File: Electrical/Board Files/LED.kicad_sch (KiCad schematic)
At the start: 22 parts, among them M1 Motor_DC, Q3 BSS138, Q4 BSS138, Q5 BSS138, Q6 BSS138, Q7 BSS138, Q8 BSS138

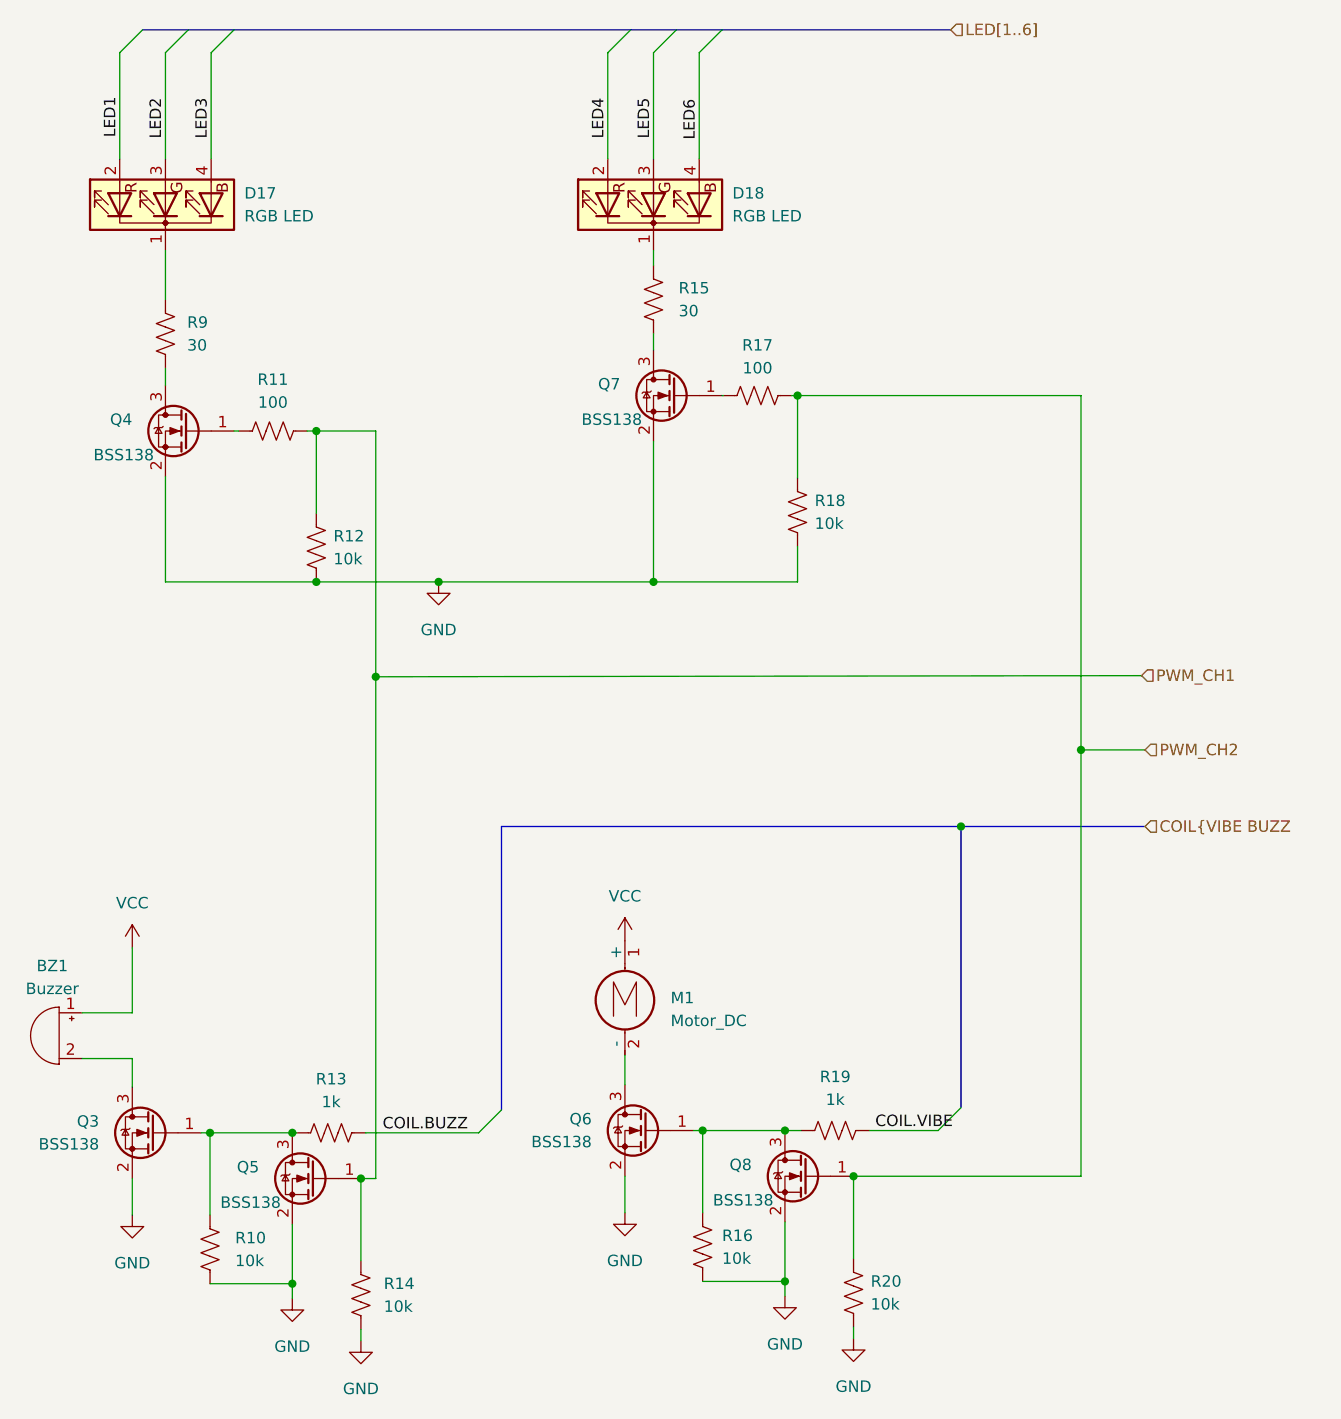
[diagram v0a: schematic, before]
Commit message: Removed unnecessary FETs
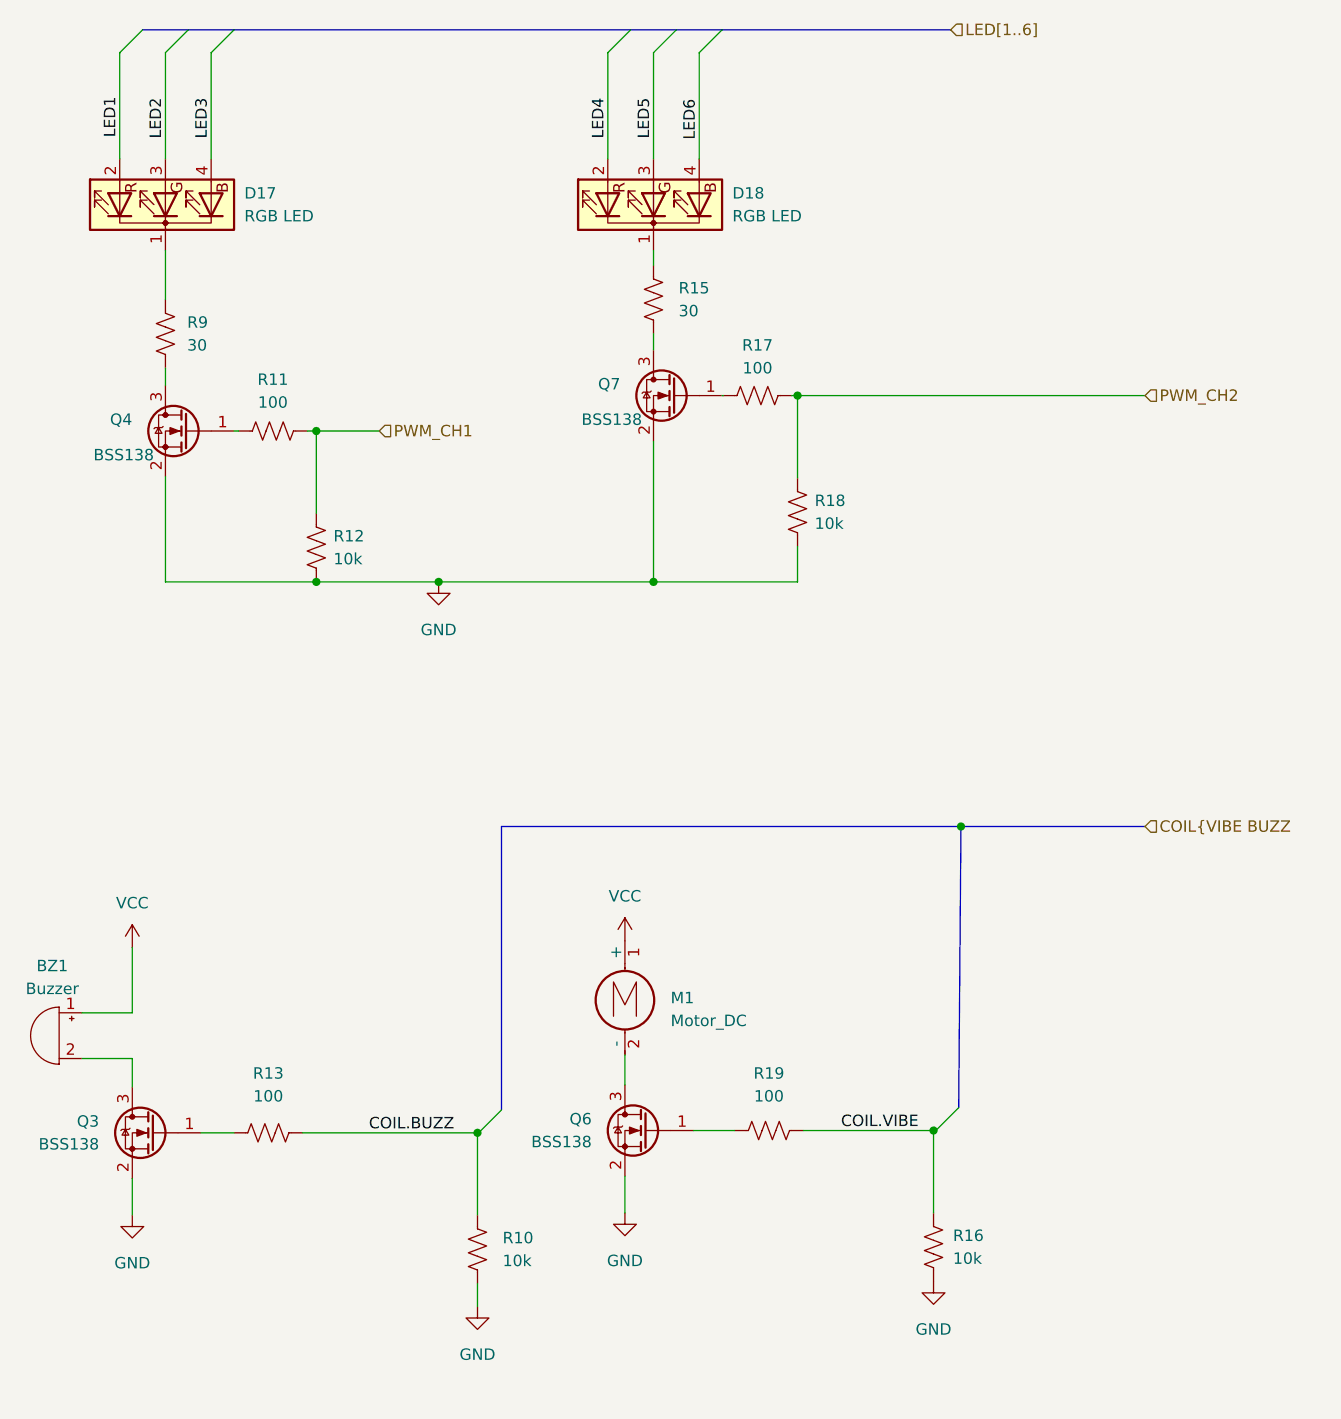
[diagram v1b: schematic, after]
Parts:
- removed Q5, Q8: BSS138, Package_TO_SOT_SMD:SOT-23, symbol Transistor_FET:BSS138
- removed R14, R20: 10k, Resistor_SMD:R_0603_1608Metric, symbol Device:R_US
- R13, R19: value 1k -> 100
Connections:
- net COIL.BUZZ: now also R10.1
- net COIL.VIBE: now also R16.1
- net at Q3.1 (G), R13.1: no longer R10.1
- net at Q6.1 (G), R19.1: no longer R16.1
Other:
- moved on the sheet: R10, R13, R16, R19

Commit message: Adding footprints
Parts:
- BZ1: footprint (none) -> Connector_PinSocket_2.00mm:PinSocket_1x02_P2.00mm_Vertical
- M1: footprint (none) -> Connector_PinSocket_2.54mm:PinSocket_1x04_P2.54mm_Vertical
- renumbered Q6 to Q5, Q7 to Q6, R9 to R15, R13 to R16, R11 to R17, R12 to R18, R10 to R19, R15 to R20, R17 to R21, R19 to R22, R18 to R23, R16 to R24
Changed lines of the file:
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@@
   (symbol (lib_id "Transistor_FET:BSS138") (at 107.442 64.389 0) (mirror y) (unit 1)
     (in_bom yes) (on_board yes)
-    (property "Reference" "Q7" (id 0) (at 101.219 63.1189 0)
+    (property "Reference" "Q6" (id 0) (at 101.219 63.1189 0)
       (effects (font (size 1.27 1.27)) (justify left))
     )
@@
   (symbol (lib_id "power:GND") (at 136.017 162.814 0) (unit 1)
     (in_bom yes) (on_board yes) (fields_autoplaced)
-    (property "Reference" "#PWR?" (id 0) (at 136.017 169.164 0)
+    (property "Reference" "#PWR044" (id 0) (at 136.017 169.164 0)
       (effects (font (size 1.27 1.27)) hide)
     )
@@
   (symbol (lib_id "power:VCC") (at 101.727 124.968 0) (unit 1)
     (in_bom yes) (on_board yes) (fields_autoplaced)
-    (property "Reference" "#PWR035" (id 0) (at 101.727 128.778 0)
+    (property "Reference" "#PWR042" (id 0) (at 101.727 128.778 0)
       (effects (font (size 1.27 1.27)) hide)
     )
@@
   (symbol (lib_id "Device:R_US") (at 136.017 159.004 0) (unit 1)
     (in_bom yes) (on_board yes) (fields_autoplaced)
-    (property "Reference" "R16" (id 0) (at 138.176 157.7339 0)
+    (property "Reference" "R24" (id 0) (at 138.176 157.7339 0)
       (effects (font (size 1.27 1.27)) (justify left))
     )
@@
   (symbol (lib_id "Transistor_FET:BSS138") (at 104.267 146.05 0) (mirror y) (unit 1)
     (in_bom yes) (on_board yes) (fields_autoplaced)
-    (property "Reference" "Q6" (id 0) (at 98.044 144.7799 0)
+    (property "Reference" "Q5" (id 0) (at 98.044 144.7799 0)
       (effects (font (size 1.27 1.27)) (justify left))
     )
@@
   (symbol (lib_id "power:GND") (at 85.344 165.608 0) (unit 1)
     (in_bom yes) (on_board yes) (fields_autoplaced)
-    (property "Reference" "#PWR032" (id 0) (at 85.344 171.958 0)
+    (property "Reference" "#PWR041" (id 0) (at 85.344 171.958 0)
       (effects (font (size 1.27 1.27)) hide)
     )
@@
   (symbol (lib_id "power:GND") (at 101.727 155.194 0) (unit 1)
     (in_bom yes) (on_board yes) (fields_autoplaced)
-    (property "Reference" "#PWR036" (id 0) (at 101.727 161.544 0)
+    (property "Reference" "#PWR043" (id 0) (at 101.727 161.544 0)
       (effects (font (size 1.27 1.27)) hide)
     )
@@
     (property "Reference" "BZ1" (id 0) (at 38.1 127.762 0))
     (property "Value" "Buzzer" (id 1) (at 38.1 130.302 0))
-    (property "Footprint" "" (id 2) (at 39.497 132.969 90)
+    (property "Footprint" "Connector_PinSocket_2.00mm:PinSocket_1x02_P2.00mm_Vertical" (id 2) (at 39.497 132.969 90)
       (effects (font (size 1.27 1.27)) hide)
     )
@@
   (symbol (lib_id "Device:R_US") (at 120.904 77.343 0) (unit 1)
     (in_bom yes) (on_board yes) (fields_autoplaced)
-    (property "Reference" "R18" (id 0) (at 122.809 76.0729 0)
+    (property "Reference" "R23" (id 0) (at 122.809 76.0729 0)
       (effects (font (size 1.27 1.27)) (justify left))
     )
@@
   (symbol (lib_id "Device:R_US") (at 104.902 53.721 0) (unit 1)
     (in_bom yes) (on_board yes) (fields_autoplaced)
-    (property "Reference" "R15" (id 0) (at 107.696 52.4509 0)
+    (property "Reference" "R20" (id 0) (at 107.696 52.4509 0)
       (effects (font (size 1.27 1.27)) (justify left))
     )
@@
   (symbol (lib_id "Device:R_US") (at 85.344 159.258 0) (unit 1)
     (in_bom yes) (on_board yes) (fields_autoplaced)
-    (property "Reference" "R10" (id 0) (at 88.138 157.9879 0)
+    (property "Reference" "R19" (id 0) (at 88.138 157.9879 0)
       (effects (font (size 1.27 1.27)) (justify left))
     )
@@
   (symbol (lib_id "Device:R_US") (at 50.673 57.531 0) (unit 1)
     (in_bom yes) (on_board yes) (fields_autoplaced)
-    (property "Reference" "R9" (id 0) (at 53.086 56.2609 0)
+    (property "Reference" "R15" (id 0) (at 53.086 56.2609 0)
       (effects (font (size 1.27 1.27)) (justify left))
     )
@@
   (symbol (lib_id "Device:R_US") (at 67.437 81.28 0) (unit 1)
     (in_bom yes) (on_board yes) (fields_autoplaced)
-    (property "Reference" "R12" (id 0) (at 69.342 80.0099 0)
+    (property "Reference" "R18" (id 0) (at 69.342 80.0099 0)
       (effects (font (size 1.27 1.27)) (justify left))
     )
@@
   (symbol (lib_id "Device:R_US") (at 116.459 64.389 90) (unit 1)
     (in_bom yes) (on_board yes) (fields_autoplaced)
-    (property "Reference" "R17" (id 0) (at 116.459 58.801 90))
+    (property "Reference" "R21" (id 0) (at 116.459 58.801 90))
     (property "Value" "100" (id 1) (at 116.459 61.341 90))
     (property "Footprint" "Resistor_SMD:R_0603_1608Metric" (id 2) (at 116.713 63.373 90)
@@
   (symbol (lib_id "power:VCC") (at 46.99 125.73 0) (unit 1)
     (in_bom yes) (on_board yes) (fields_autoplaced)
-    (property "Reference" "#PWR030" (id 0) (at 46.99 129.54 0)
+    (property "Reference" "#PWR038" (id 0) (at 46.99 129.54 0)
       (effects (font (size 1.27 1.27)) hide)
     )
@@
   (symbol (lib_id "Device:R_US") (at 62.103 146.304 90) (unit 1)
     (in_bom yes) (on_board yes) (fields_autoplaced)
-    (property "Reference" "R13" (id 0) (at 62.103 139.7 90))
+    (property "Reference" "R16" (id 0) (at 62.103 139.7 90))
     (property "Value" "100" (id 1) (at 62.103 142.24 90))
     (property "Footprint" "Resistor_SMD:R_0603_1608Metric" (id 2) (at 62.357 145.288 90)
@@
   (symbol (lib_id "power:GND") (at 46.99 155.448 0) (unit 1)
     (in_bom yes) (on_board yes) (fields_autoplaced)
-    (property "Reference" "#PWR031" (id 0) (at 46.99 161.798 0)
+    (property "Reference" "#PWR039" (id 0) (at 46.99 161.798 0)
       (effects (font (size 1.27 1.27)) hide)
     )
@@
   (symbol (lib_id "Device:R_US") (at 62.611 68.326 90) (unit 1)
     (in_bom yes) (on_board yes) (fields_autoplaced)
-    (property "Reference" "R11" (id 0) (at 62.611 62.611 90))
+    (property "Reference" "R17" (id 0) (at 62.611 62.611 90))
     (property "Value" "100" (id 1) (at 62.611 65.151 90))
     (property "Footprint" "Resistor_SMD:R_0603_1608Metric" (id 2) (at 62.865 67.31 90)
@@
   (symbol (lib_id "Device:R_US") (at 117.729 146.05 90) (unit 1)
     (in_bom yes) (on_board yes) (fields_autoplaced)
-    (property "Reference" "R19" (id 0) (at 117.729 139.7 90))
+    (property "Reference" "R22" (id 0) (at 117.729 139.7 90))
     (property "Value" "100" (id 1) (at 117.729 142.24 90))
     (property "Footprint" "Resistor_SMD:R_0603_1608Metric" (id 2) (at 117.983 145.034 90)
@@
       (effects (font (size 1.27 1.27)) (justify left))
     )
-    (property "Footprint" "" (id 2) (at 101.727 132.334 0)
+    (property "Footprint" "Connector_PinSocket_2.54mm:PinSocket_1x04_P2.54mm_Vertical" (id 2) (at 101.727 132.334 0)
       (effects (font (size 1.27 1.27)) hide)
     )
@@
   (symbol (lib_id "power:GND") (at 81.026 85.09 0) (unit 1)
     (in_bom yes) (on_board yes) (fields_autoplaced)
-    (property "Reference" "#PWR034" (id 0) (at 81.026 91.44 0)
-      (effects (font (size 1.27 1.27)) hide)
-    )
+    (property "Reference" "#PWR040" (id 0) (at 81.026 91.44 0)
+      (effects (font (size 1.27 1.27)) hide)
+    )
